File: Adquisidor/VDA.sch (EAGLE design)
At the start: 137 parts, among them J1 USB-2.0, J2 CONVERT-1X4-2.54MM-MALE_HOLES, J3 FTSH-107-01-L-DV-K-A, J4 STEREO-JACK, J5 F0504-H-05-10G-R, J6 CONVERT-2X7-2.54MM-FEMALE, Q1 BC856, Q2 BC856, SW1 DSHP03TSGER, U1 CP2102N-28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

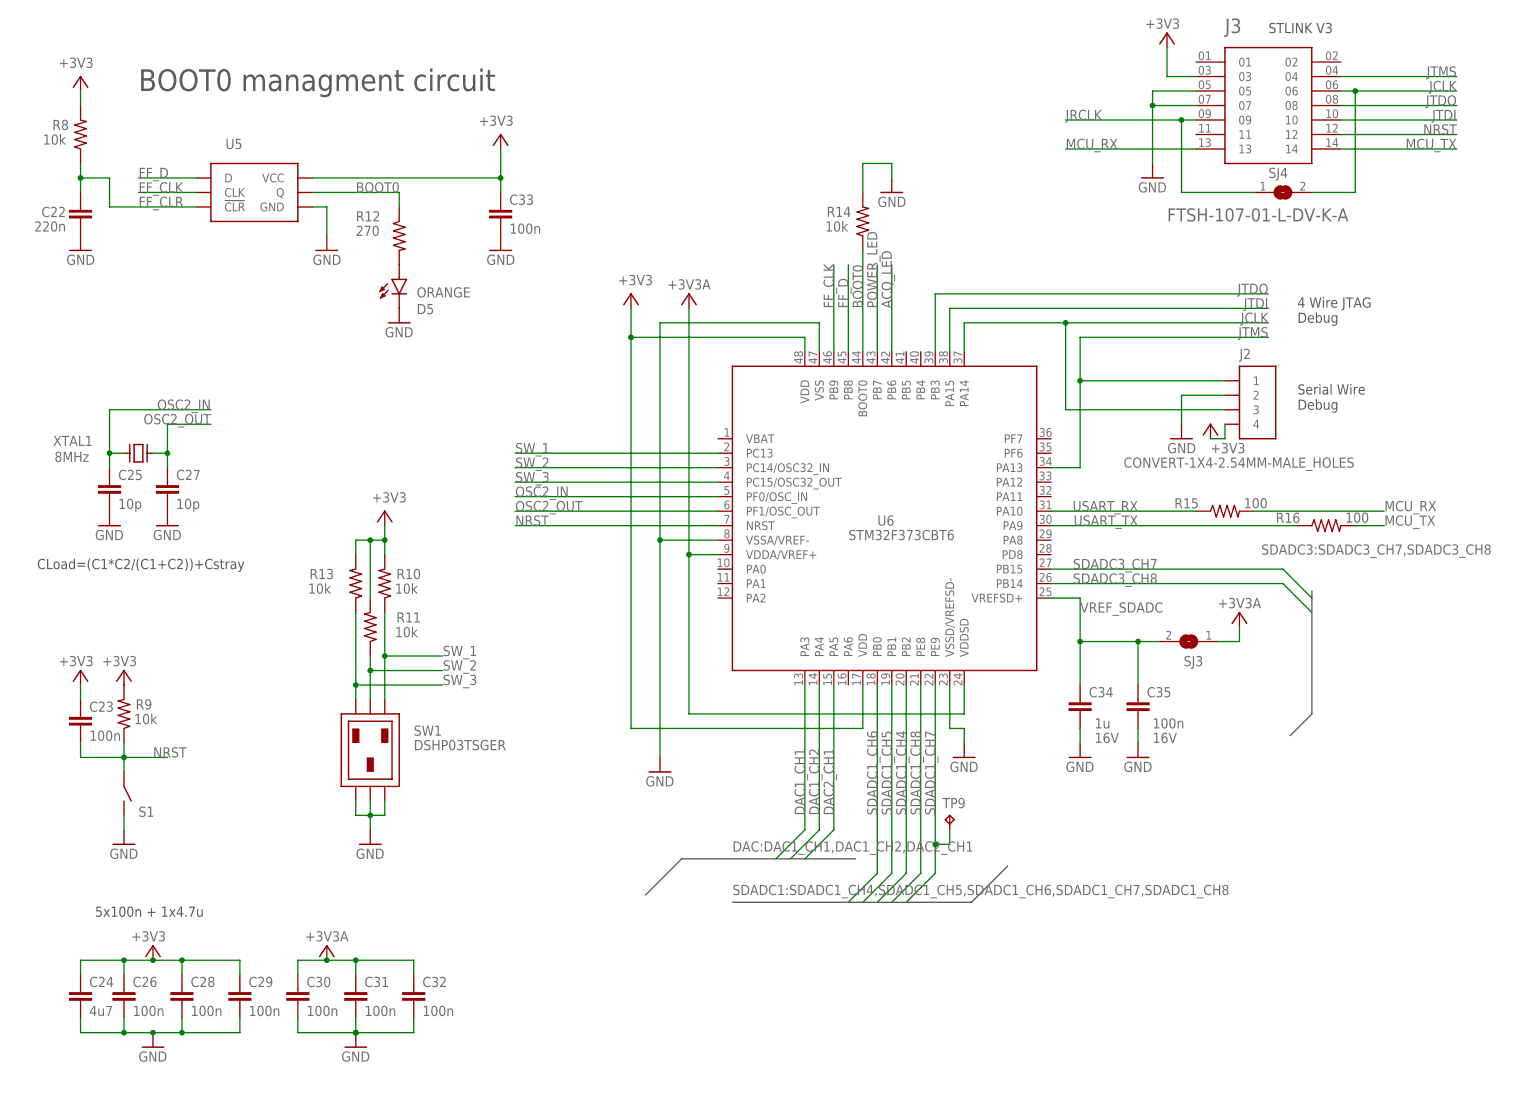
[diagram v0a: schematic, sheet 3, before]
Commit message: added README file
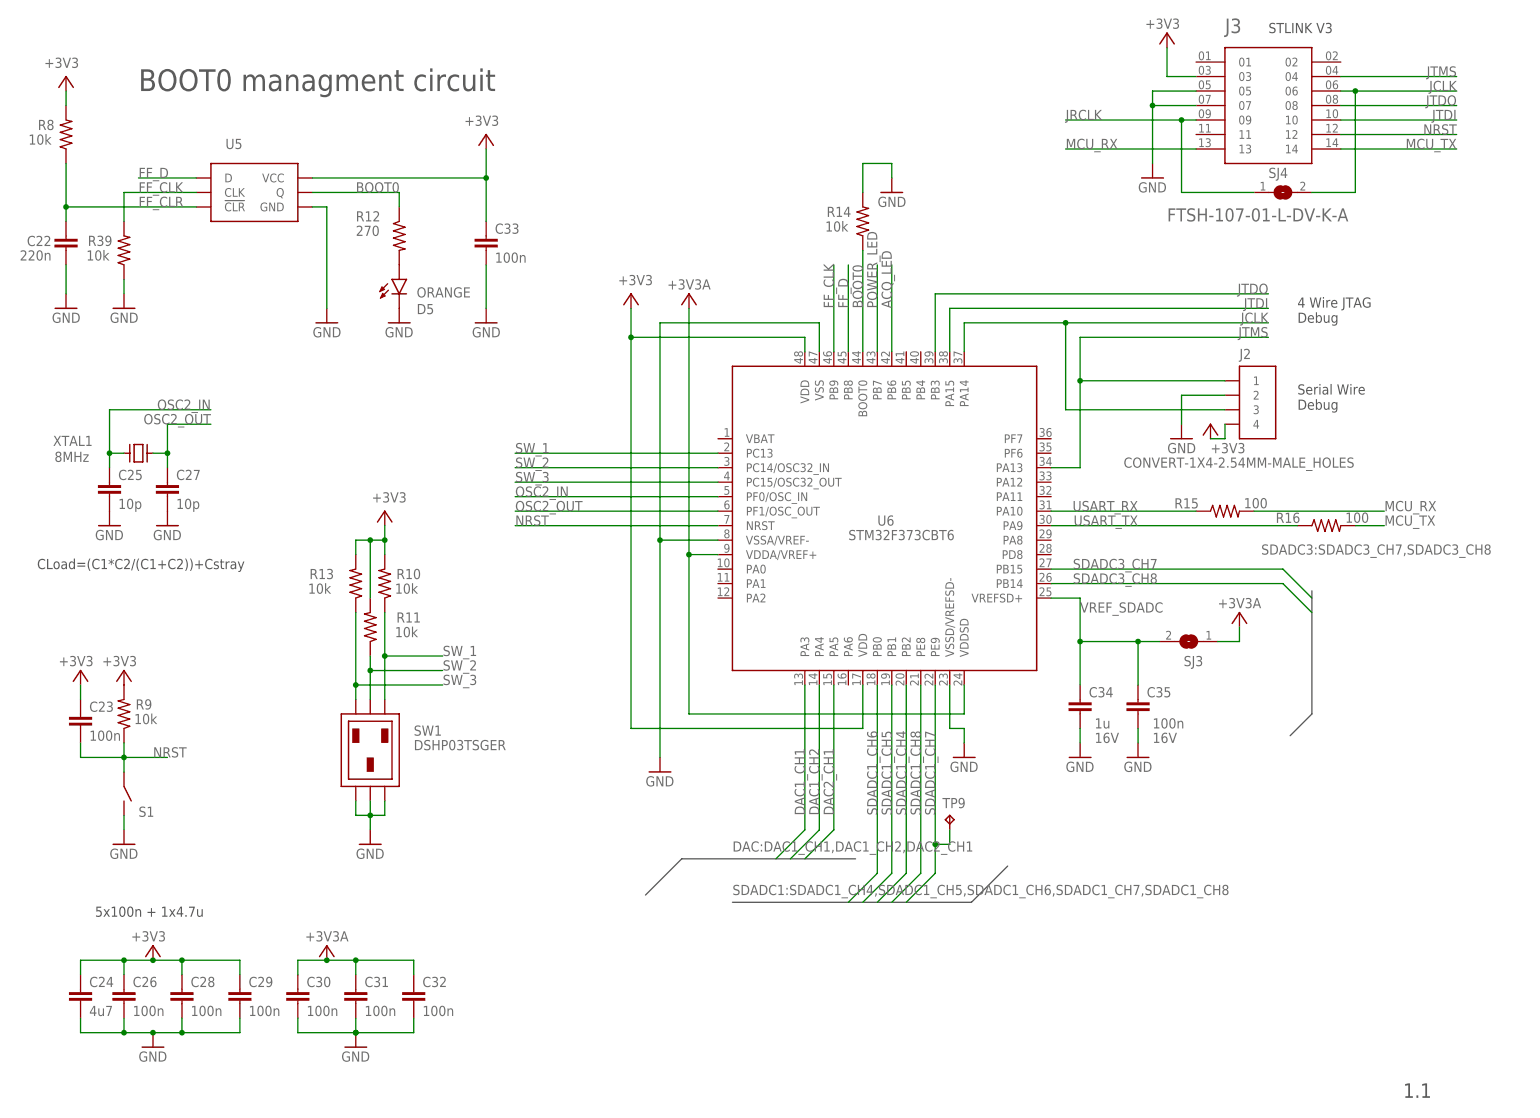
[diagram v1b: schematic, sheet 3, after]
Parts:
- added R39: 10k, Property-standar:R_0603
- R17: value DNP -> 510k
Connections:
- net FF_CLK: now also R39.2
- net GND: now also R39.1
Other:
- note added: "(0-3V3 -> 6.5-100uA)"
- note added: "100000 V/A"
- note added: "Gain 6.5x10e-6 - 93.8x10e-6 A/V"
- note removed: "(0-3V3 -> 0-100uA)"
- note removed: "Ganancia 0.16 - 2.5"
- moved on the sheet: C22, C33, R8
